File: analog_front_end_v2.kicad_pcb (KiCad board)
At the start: 4 copper layers, 155 parts, among them J1 Conn_Coaxial, J3 Conn_01x01_Socket, J4 Conn_01x01_Socket, U1 ADL5531, U10 PMOD 2x6, U11 LP2985-5.0, U12 LP2985-5.0, U13 LT1363, U14 MAX 735, U15 LP2985-2.5, U16 MAX889SESA, U17 MAX6102, U2 ADL5531, U3 ADL5531, U4 PE4140B-Z, U5 ADF4360-9, U6 LTC1406, U7 THS4551, U8 LT1363, U9 PMOD 2x6

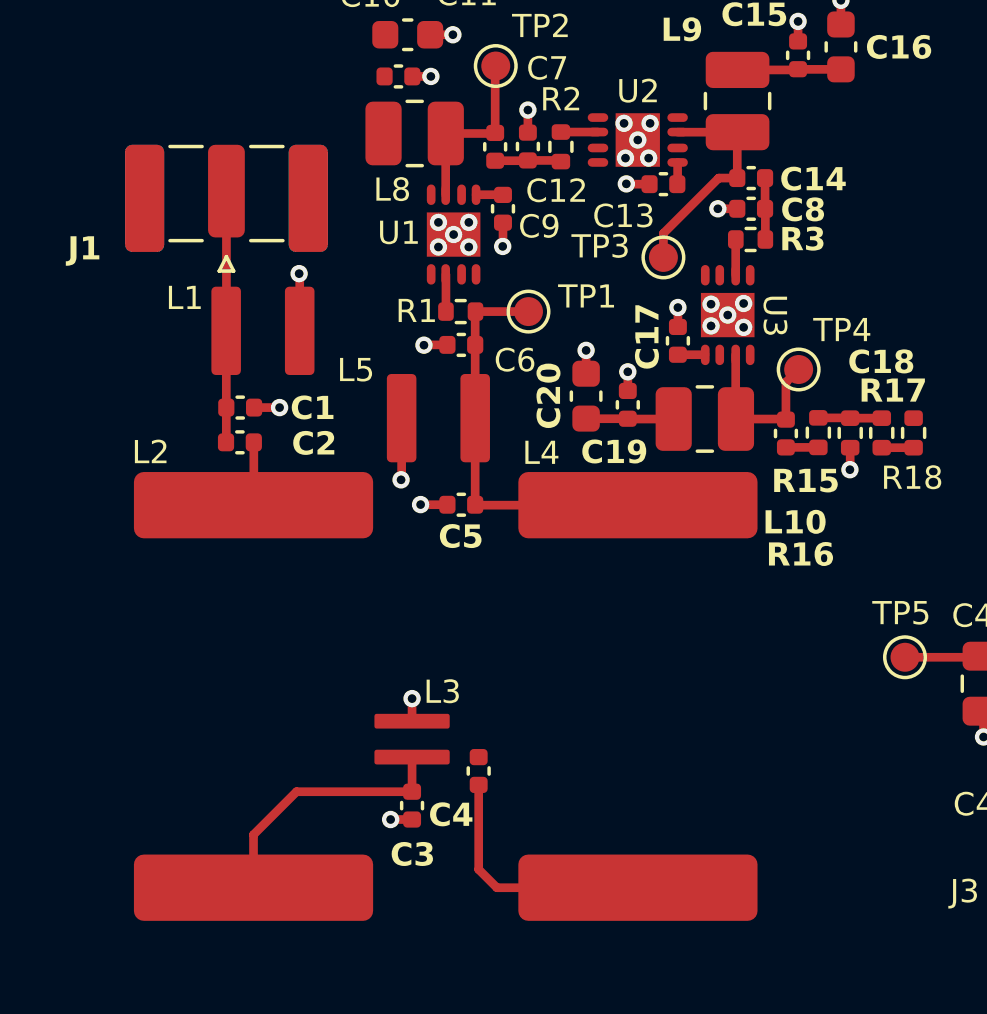
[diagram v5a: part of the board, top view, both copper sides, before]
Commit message: Update notes/decisions in schematics/pcb for clarity
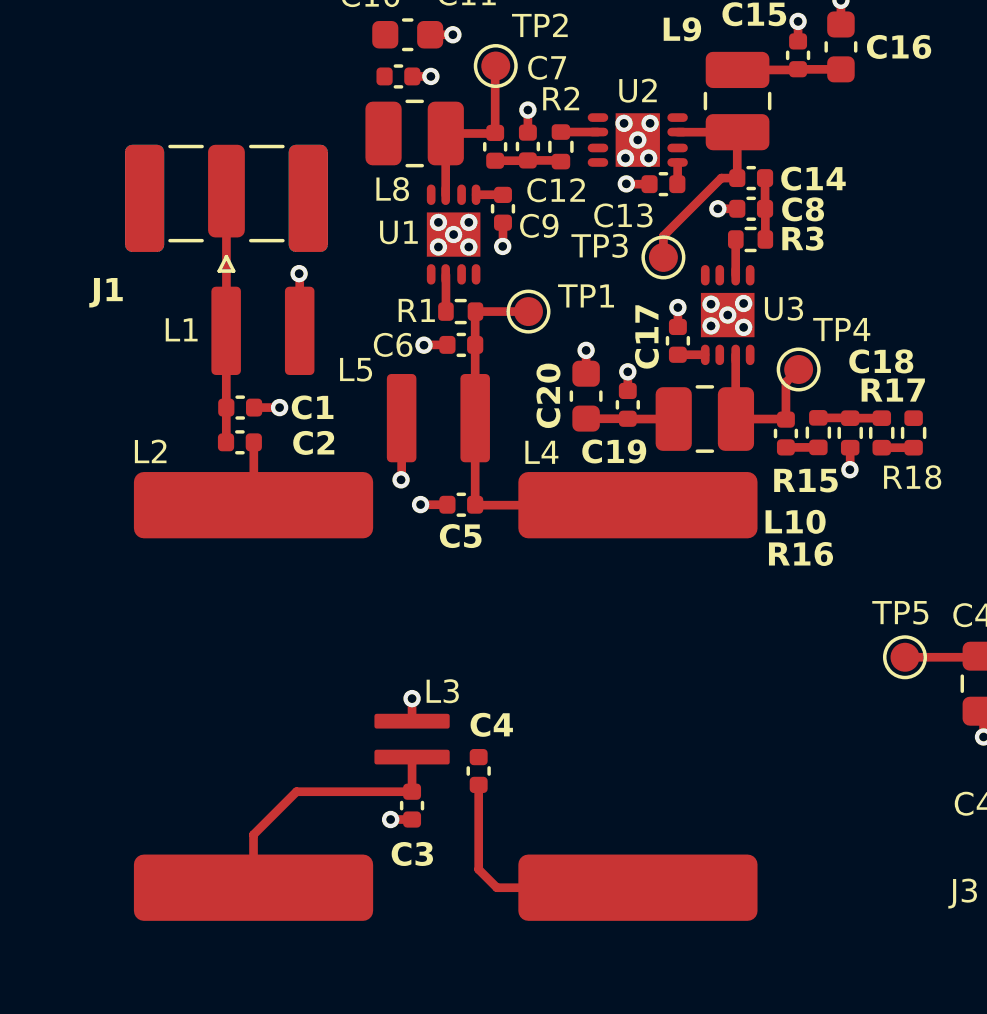
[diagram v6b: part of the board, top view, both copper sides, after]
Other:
- board text added: "TODO: Ground via stitching Decisions: Use 0.3mm trace for 50ohm characteristic impedance for microstrip with solid groundplane Use 0.8mm silkscreen height for improved readability"
- board text removed: "TODO: Ground via stitching Use 0.3mm trace for 50ohm characteristic impedance for microstrip with solid groundplane Use 0.8mm silkscreen height for improved readability"
- board text removed: "TODO: Layout L2/L4 to cancel out mutual inductances"
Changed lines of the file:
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@@
 		(at 18.45 24.825)
 		(property "Reference" "L1"
-			(at -2.7 -1.125 0)
+			(at -2.81 -0.005 0)
 			(unlocked yes)
 			(layer "F.SilkS")
@@
 		(at 34.5 24.28 -90)
 		(property "Reference" "U3"
-			(at 0.02 -1.62 270)
+			(at -0.19 -1.94 0)
 			(unlocked yes)
 			(layer "F.SilkS")
@@
 		(tags "capacitor")
 		(property "Reference" "C4"
-			(at 1.525 0.95 180)
+			(at -1.565 -0.45 180)
 			(layer "F.SilkS")
 			(effects
@@
 		(tags "capacitor")
 		(property "Reference" "C6"
-			(at -1.86 -0.54 180)
+			(at 2.35 -0.03 180)
 			(layer "F.SilkS")
 			(effects
@@
 		(tags "SMA Straight Samtec Edge Mount")
 		(property "Reference" "J1"
-			(at -1.9875 -4.9 0)
+			(at -3.43 -4.09 0)
 			(layer "F.SilkS")
 			(effects
@@
 		(layer "Margin")
 	)
-	(gr_text "TODO: Layout L2/L4 to cancel out mutual inductances"
-		(at 57 6.3 0)
-		(layer "Cmts.User")
-		(effects
-			(font
-				(size 0.8 0.8)
-				(thickness 0.1)
-			)
-		)
-	)
 	(gr_text "12V DC IN from benchtop power supply and GND"
 		(at 118.875 59.555 0)
@@
 		)
 	)
-	(gr_text "TODO: Ground via stitching\nUse 0.3mm trace for 50ohm characteristic impedance \nfor microstrip with solid groundplane\nUse 0.8mm silkscreen height for improved readability"
+	(gr_text "TODO: \nGround via stitching\nDecisions:\nUse 0.3mm trace for 50ohm characteristic impedance \nfor microstrip with solid groundplane\nUse 0.8mm silkscreen height for improved readability"
 		(at 31.6 2.1 0)
 		(layer "Cmts.User")
@@
 	)
 	(segment
-		(start 34.83 19.55)
-		(end 34.19 19.55)
+		(start 32.28 21.55)
+		(end 32.28 22.29)
 		(width 0.3)
 		(layer "F.Cu")
@@
 	)
 	(segment
-		(start 32.775 17.965)
-		(end 32.77 17.96)
-		(width 0.2)
+		(start 34.83 19.55)
+		(end 34.28 19.55)
+		(width 0.3)
 		(layer "F.Cu")
 		(net 13)
 	)
 	(segment
-		(start 34.19 19.55)
-		(end 32.28 21.46)
-		(width 0.3)
+		(start 32.775 17.965)
+		(end 32.77 17.96)
+		(width 0.2)
 		(layer "F.Cu")
 		(net 13)
 	)
 	(segment
-		(start 32.28 21.46)
-		(end 32.28 22.29)
+		(start 34.83 19.55)
+		(end 34.83 17.975)
 		(width 0.3)
 		(layer "F.Cu")
@@
 	)
 	(segment
-		(start 34.83 19.55)
-		(end 34.83 17.975)
+		(start 34.28 19.55)
+		(end 32.28 21.55)
 		(width 0.3)
 		(layer "F.Cu")

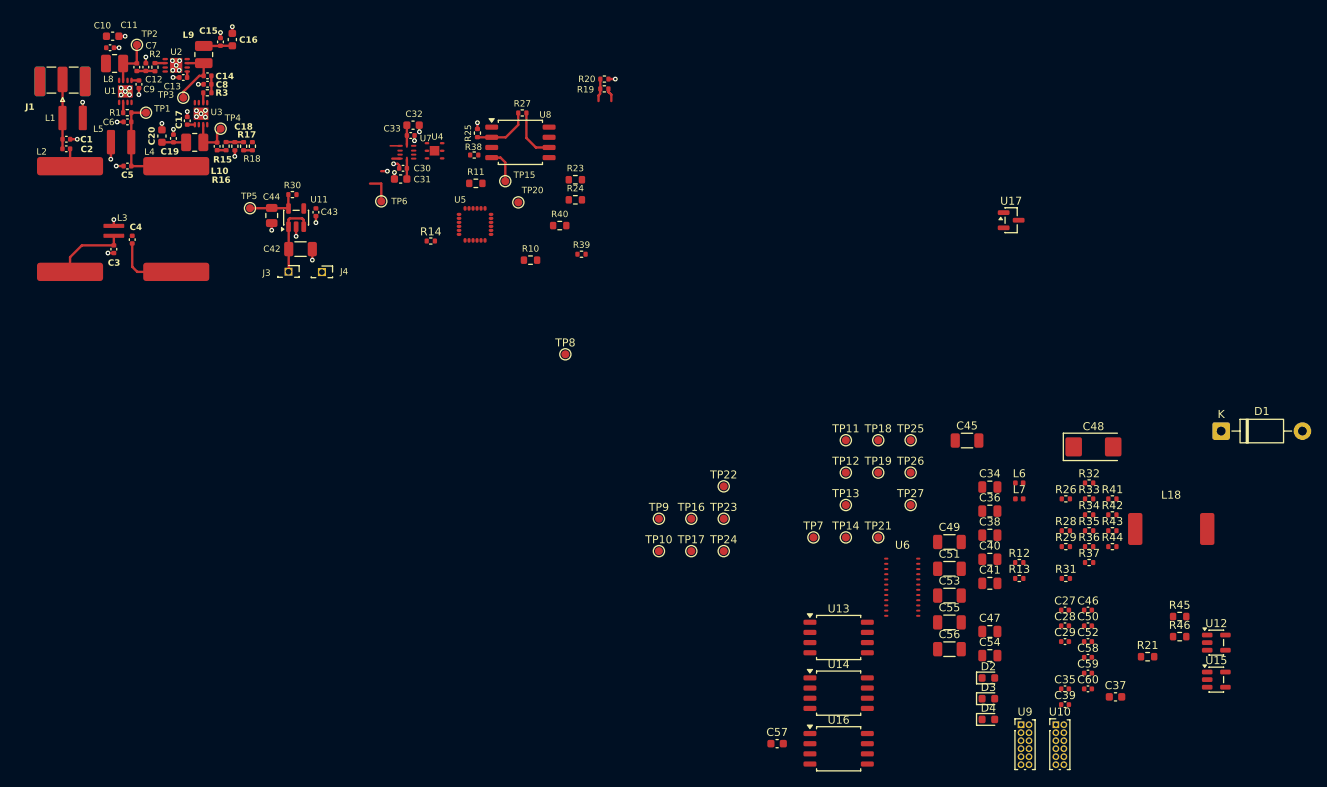
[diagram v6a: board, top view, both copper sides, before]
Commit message: Reduce size of all silkscreen to 0.4mm for easier placement
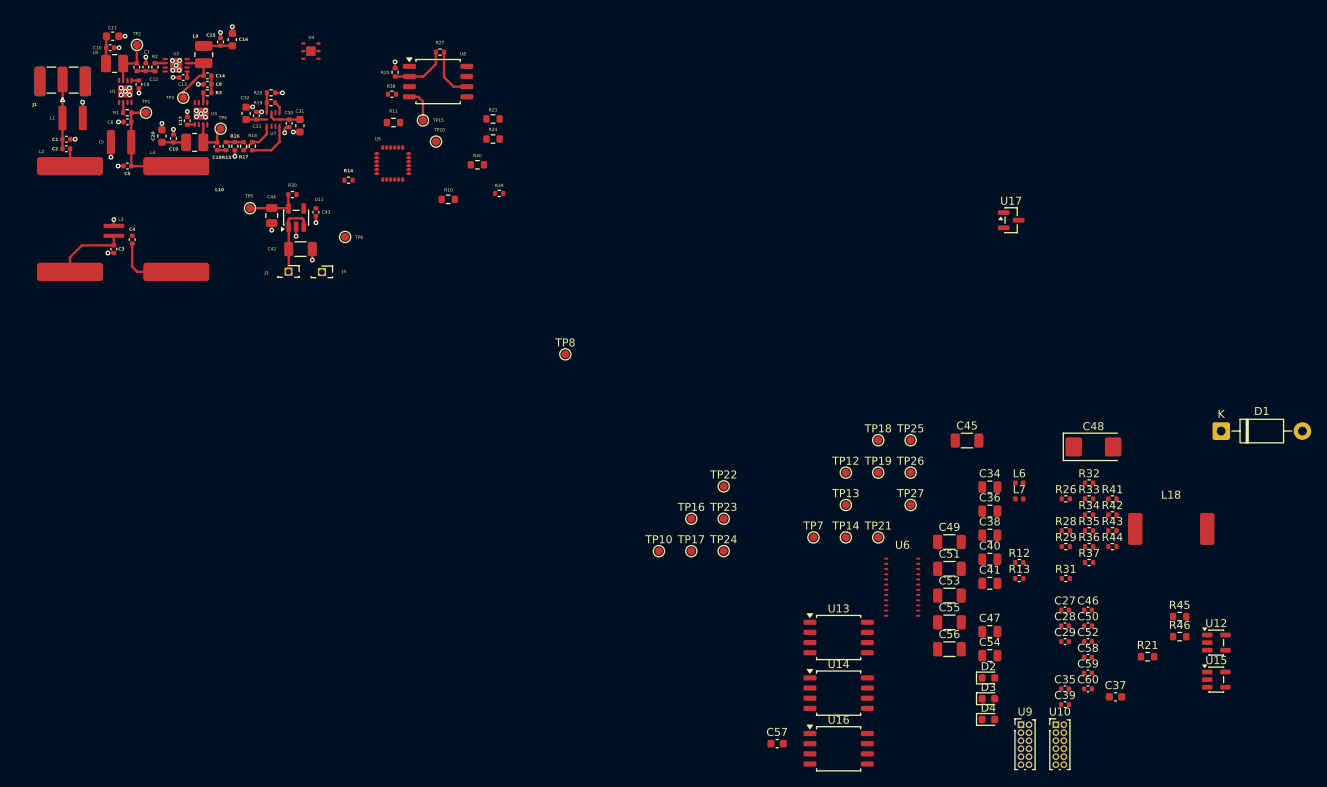
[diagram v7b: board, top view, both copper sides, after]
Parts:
- removed TP11, TP9: TestPoint, TestPoint:TestPoint_Pad_D1.0mm
- C30, C33: value 0.1uF -> 0.1u_10V
- C31, C32: value 2.2uF -> 2.2uF_25V
- C34, C36, C38, C40, C41, C49, C51: value 10uF -> 10u_16V
- C35: value 56pF -> 56p_50V
- C37: value 2.2nF -> 2.2n_50V
- C39: value 150pF -> 150p_150V
- C48: value 47uF -> 47u_16V
- C55, C56: value 4.7uF -> 4.7u_16V
- C57: value 1uF -> 1u_16V
- moved R19 41.7 mm to (43.2, 22.9)
- moved R20 41.7 mm to (43.2, 21.7)
- moved C32 20.9 mm to (40.1, 24.2), turned to -90 degrees
- moved U4 19.9 mm to (48.2, 16.5)
- moved C33 19.4 mm to (41.4, 24.5), turned to -90 degrees
- moved U7 17.2 mm to (43.5, 25.0), turned to -90 degrees
- moved C30 15.3 mm to (45.5, 25.5), turned to 90 degrees
- moved C31 14.2 mm to (46.9, 25.8), turned to 90 degrees
- moved R10 12.8 mm to (65.4, 35.0)
- moved R39 12.8 mm to (71.8, 34.2)
- moved U8 12.8 mm to (64.1, 20.3)
- moved R23 12.8 mm to (71.0, 24.9)
- moved R24 12.8 mm to (71.0, 27.4)
- moved R38 12.8 mm to (58.4, 21.9)
- moved R14 12.8 mm to (52.9, 32.6)
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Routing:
- net DIFF_OUTP: track 1.02 -> 5.78 mm
- net DIFF_IN-: track 2.34 -> 4.76 mm
- net 2.5V_DiffAmp: track 2.45 -> 4.23 mm
- net GND: track 27.6 -> 25.9 mm, vias 45 -> 44
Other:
- board text added: "TODO: Ground via stitching Decisions: Use 0.3mm trace for 50ohm characteristic impedance for microstrip with solid groundplane Use 0.4mm silkscreen width/height to balance readability/placement Ensure RF Mixer (U4) is far away from sensitive RF/analog front end"
- board text removed: "TODO: Ground via stitching Decisions: Use 0.3mm trace for 50ohm characteristic impedance for microstrip with solid groundplane Use 0.8mm silkscreen height for improved readability"
